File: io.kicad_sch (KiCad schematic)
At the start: 22 parts, among them J10 SERVO3_CONN, J11 SWITCH4_CONN, J12 SERVO4_CONN, J13 SWITCH5_CONN, J14 SERVO5_CONN, J16 SERVO1_CONN, J2 SERVO0_CONN, J3 SWITCH0_CONN, J5 SWITCH1_CONN, J6 LID_SERVO_CONN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

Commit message: Add testpoints
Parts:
- C24, C27: now left out of the parts list
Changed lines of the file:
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@@
 		(body_style 1)
 		(exclude_from_sim no)
-		(in_bom yes)
+		(in_bom no)
 		(on_board yes)
 		(in_pos_files yes)
@@
 		(body_style 1)
 		(exclude_from_sim no)
-		(in_bom yes)
-		(on_board yes)
-		(in_pos_files yes)
+		(in_bom no)
+		(on_board yes)
+		(in_pos_files yes)

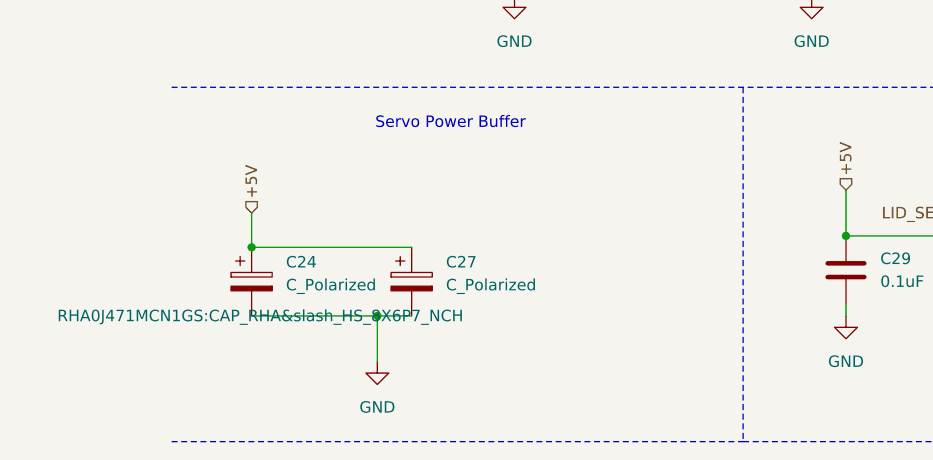
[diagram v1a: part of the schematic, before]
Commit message: Fix some bugs in the circuit
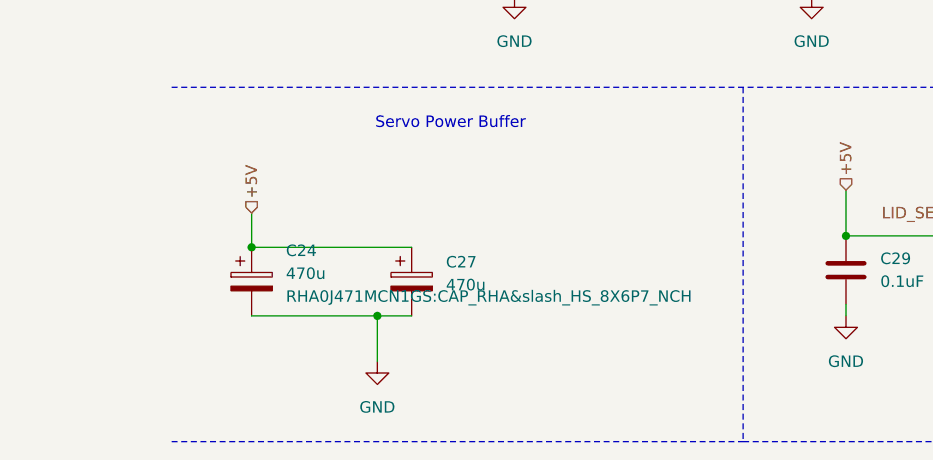
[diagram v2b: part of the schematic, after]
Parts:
- C24, C27: value C_Polarized -> 470u
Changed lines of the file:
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@@
 		(fields_autoplaced yes)
 		(property "Reference" "C24"
-			(at 24.13 108.3309 0)
+			(at 24.13 107.0609 0)
 			(show_name no)
 			(do_not_autoplace no)
@@
 			)
 		)
-		(property "Value" "C_Polarized"
-			(at 24.13 110.8709 0)
+		(property "Value" "470u"
+			(at 24.13 109.6009 0)
 			(show_name no)
 			(do_not_autoplace no)
@@
 		)
 		(property "Footprint" "RHA0J471MCN1GS:CAP_RHA&slash_HS_8X6P7_NCH"
-			(at 21.2852 114.3 0)
-			(show_name no)
-			(do_not_autoplace no)
-			(effects
-				(font
-					(size 1.27 1.27)
-				)
+			(at 24.13 112.1409 0)
+			(show_name no)
+			(do_not_autoplace no)
+			(effects
+				(font
+					(size 1.27 1.27)
+				)
+				(justify left)
 			)
 		)
@@
 			)
 		)
-		(property "Value" "C_Polarized"
+		(property "Value" "470u"
 			(at 41.91 110.8709 0)
 			(show_name no)
